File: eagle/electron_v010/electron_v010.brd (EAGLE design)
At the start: 20.3 x 50.8 mm, 92 parts, among them J1 SIM-NANO-4FF, J2 IPEX-20279-001E, U1 U-BLOX-SARA-U260, U2 SN74AVC4T245, U3 STM32F205RG, U4 MAX1704X, U5 SN74LVC1G07, U6 SN74LVC1G07, U8 SN74AVC4T245, X1 USB-MICROB, Y1 32Khz, Y2 26Mhz

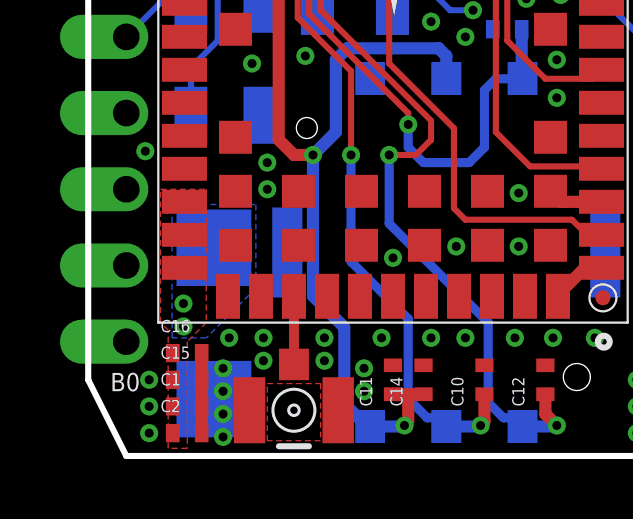
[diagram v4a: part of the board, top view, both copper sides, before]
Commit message: Added more Vias on u-blox 3.8V trace connection (PCB Ver: 010 Ready)
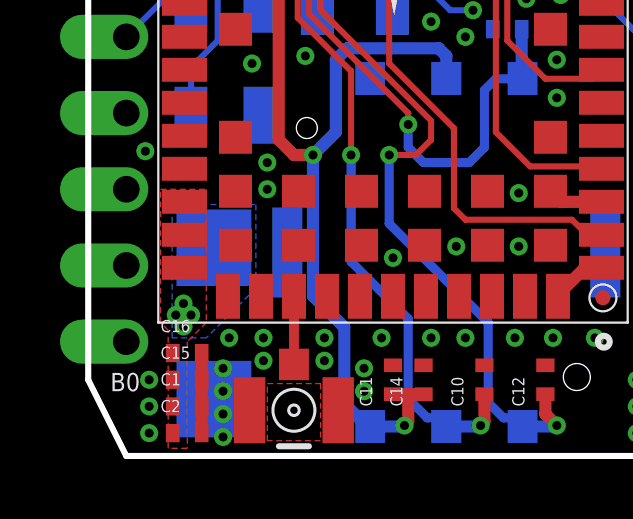
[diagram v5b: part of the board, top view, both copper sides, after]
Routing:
- net +3V8: vias 10 -> 12
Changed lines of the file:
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@@
 <vertex x="8.5344" y="44.2214"/>
 </polygon>
+<via x="3.429" y="4.699" extent="1-16" drill="0.3"/>
+<via x="2.921" y="4.699" extent="1-16" drill="0.3"/>
 </signal>
 <signal name="SIM_VCC">
